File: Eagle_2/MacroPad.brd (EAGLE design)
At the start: 70.8 x 62.2 mm, 40 parts, among them SW00 SWITCH-SMD-EVQP-P2602W, SW01 KEYSWITCH-PLAIN-MX-1U, SW02 KEYSWITCH-PLAIN-MX-1U, SW03 KEYSWITCH-PLAIN-MX-1U, SW04 KEYSWITCH-PLAIN-MX-1U, SW05 KEYSWITCH-PLAIN-MX-1U, SW06 KEYSWITCH-PLAIN-MX-1U, SW07 KEYSWITCH-PLAIN-MX-1U, SW08 KEYSWITCH-PLAIN-MX-1U, SW09 KEYSWITCH-PLAIN-MX-1U, SW10 KEYSWITCH-PLAIN-MX-1U, SW11 KEYSWITCH-PLAIN-MX-1U, SW12 KEYSWITCH-PLAIN-MX-1U

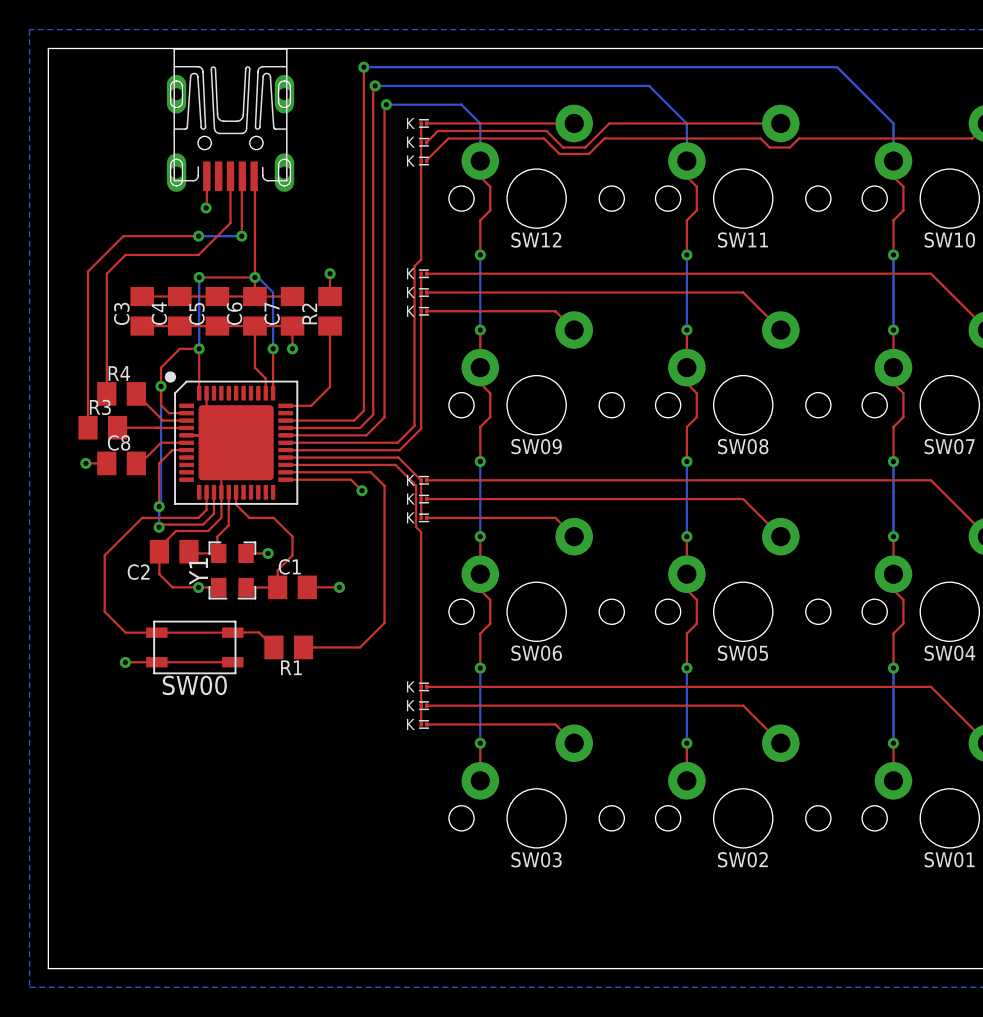
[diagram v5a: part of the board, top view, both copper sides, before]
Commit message: Components routed in compressed area
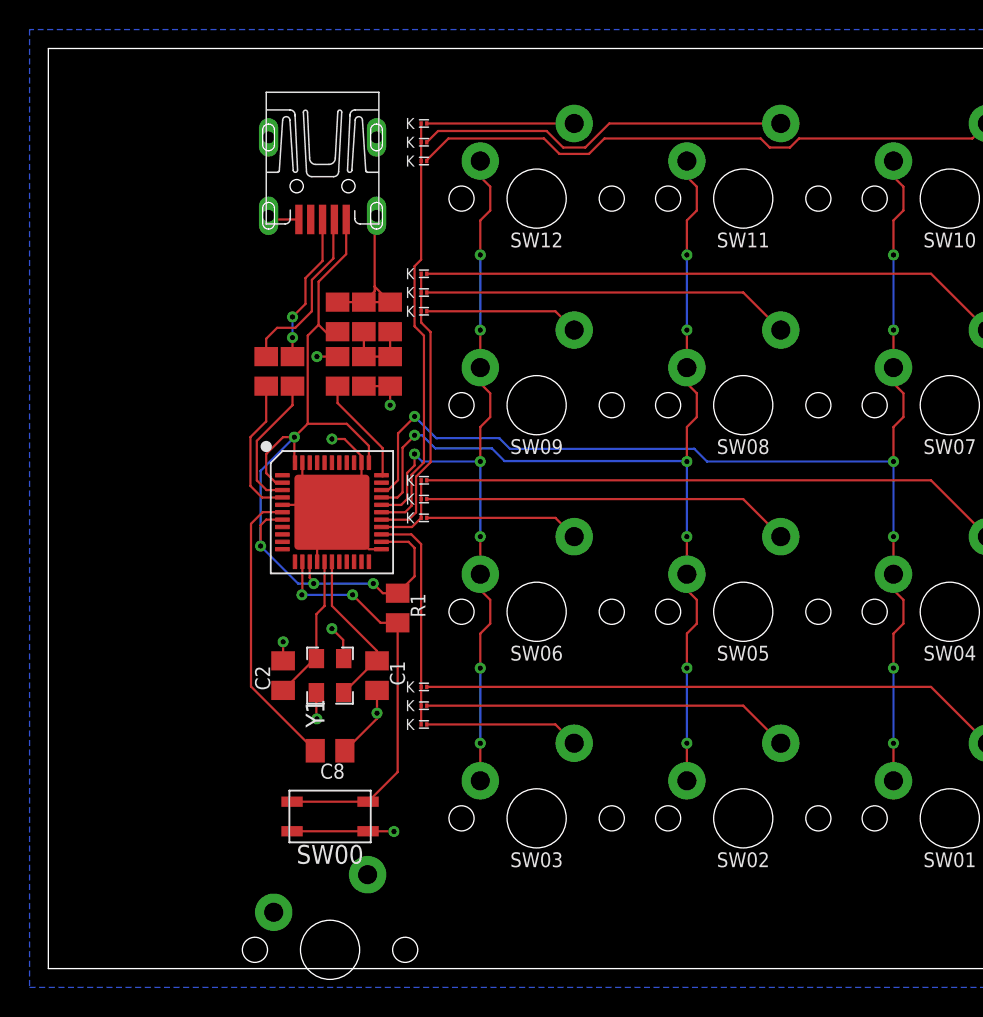
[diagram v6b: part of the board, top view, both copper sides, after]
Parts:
- added U$2: KEYSWITCH-PLAIN-MX-1U, Keyboard:MX-1U
- moved C8 24.0 mm to (19.1, 14.7), turned to 180 degrees
- moved C3 15.0 mm to (21.3, 44.1), turned to 270 degrees
- moved SW00 14.6 mm to (19.1, 10.3)
- moved C4 14.2 mm to (23.1, 44.1), turned to 270 degrees
- moved R3 11.7 mm to (14.7, 40.4), turned to 270 degrees
- moved R4 11.7 mm to (16.5, 40.4), turned to 270 degrees
- moved C2 11.2 mm to (15.9, 19.8), turned to 90 degrees
- moved Y1 9.71 mm to (19.1, 19.8)
- moved C6 8.41 mm to (21.3, 40.4)
- moved C1 8.26 mm to (22.2, 19.8), turned to 270 degrees
- moved C5 8.14 mm to (19.6, 44.1), turned to 270 degrees
- moved U$1 8.00 mm to (19.2, 30.9)
- moved R1 7.83 mm to (23.6, 24.4), turned to 270 degrees
- moved C7 7.75 mm to (23.1, 40.4)
- moved USB1 6.87 mm to (18.5, 59.3)
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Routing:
- net N$10: track 112.3 -> 83.5 mm
- net N$40: track 96.8 -> 68.5 mm
- net N$16: track 81.4 -> 53.4 mm
- net VCC: track 88.5 -> 65.5 mm, vias 7 -> 4
- net UCAP: track 3.98 -> 19.6 mm
- net N$7: track 26.0 -> 11.9 mm, vias 2 -> 0
- net N$5: track 21.1 -> 10.1 mm, vias 0 -> 2
- net N$14: track 25.7 -> 15.1 mm
- net N$26: track 12.3 -> 5.48 mm
- net N$6: track 4.14 -> 9.75 mm
- net N$8: track 5.07 -> 9.68 mm
- net UGND: track 64.0 -> 60.0 mm, vias 9 -> 8
- net N$1: track 6.55 -> 10.0 mm
- net N$3: track 25.6 -> 27.6 mm, vias 0 -> 2
- net N$38: track 29.8 -> 28.9 mm
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
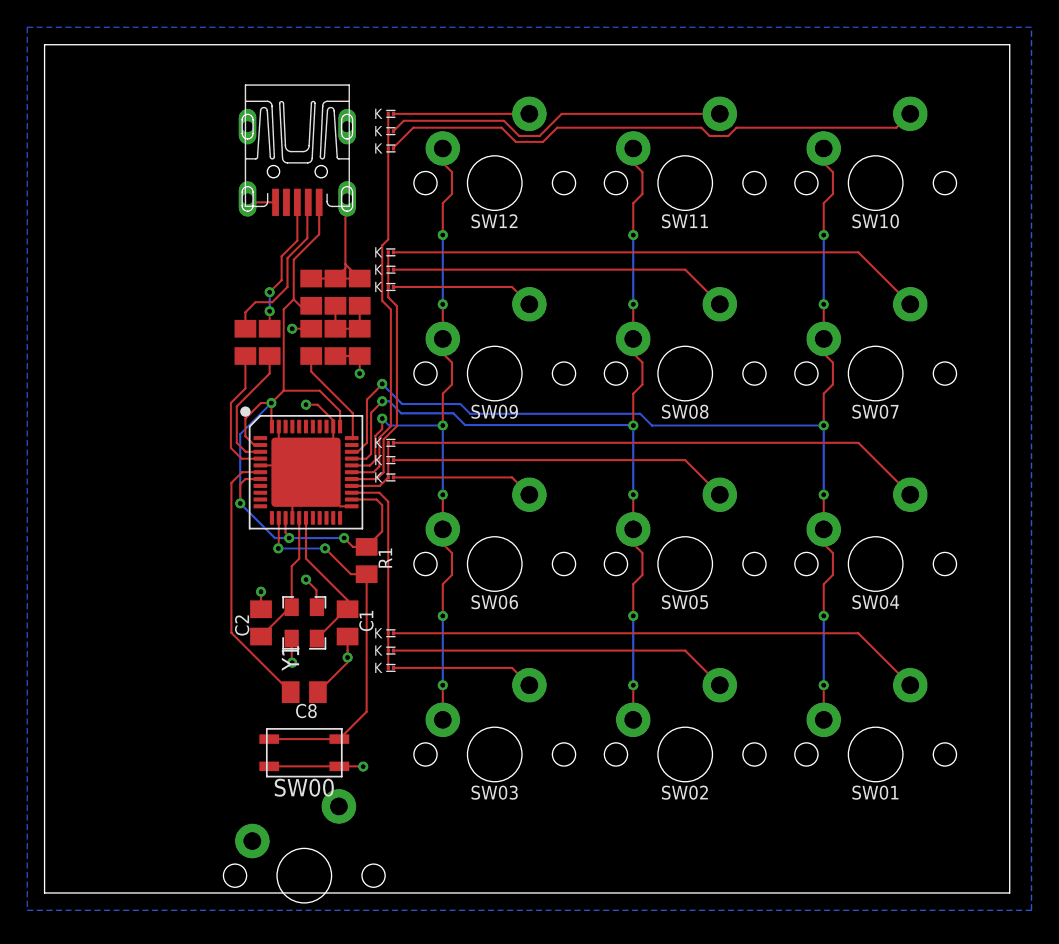
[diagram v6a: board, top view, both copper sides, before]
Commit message: Shrink board
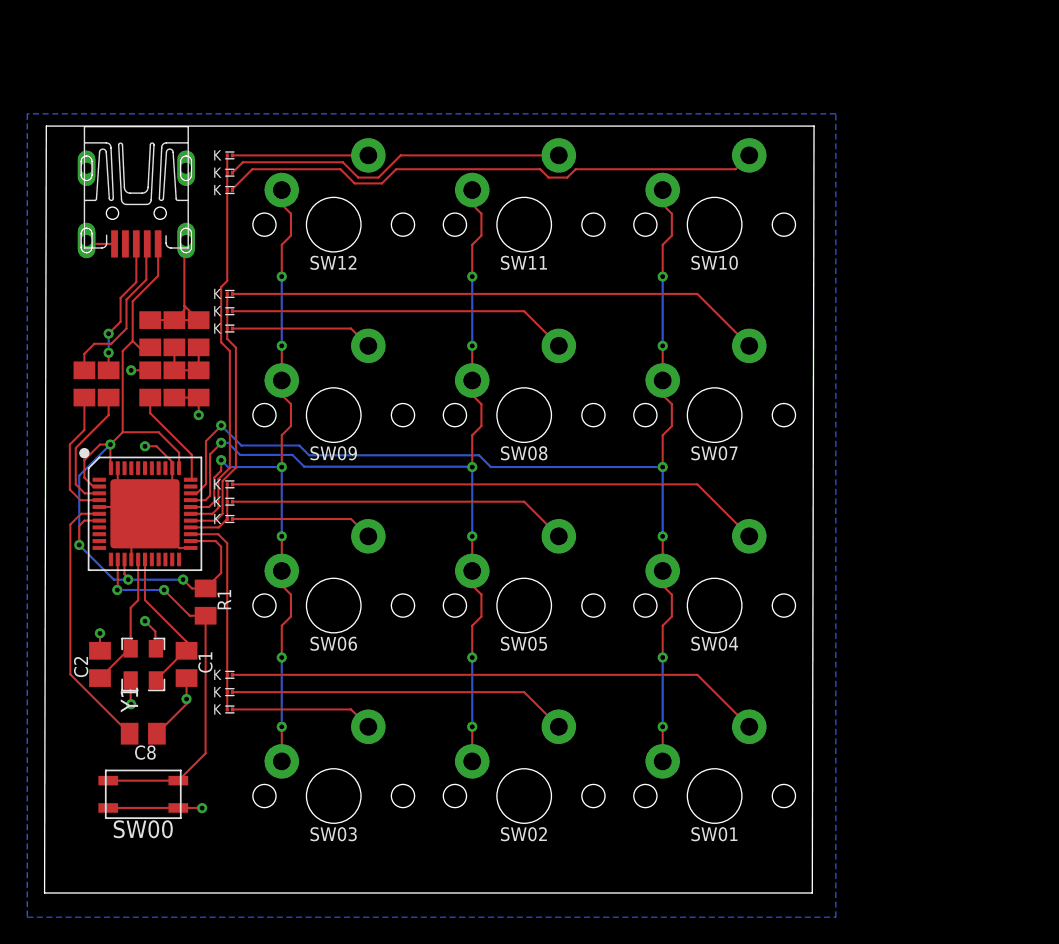
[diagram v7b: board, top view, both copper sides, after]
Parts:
- removed U$2: KEYSWITCH-PLAIN-MX-1U, Keyboard:MX-1U
- moved SW03 12.2 mm to (21.2, 7.11)
- moved SW09 12.2 mm to (21.2, 35.1)
- moved SW12 12.2 mm to (21.2, 49.0)
- moved C1 12.2 mm to (10.4, 16.8)
- moved R4 12.2 mm to (4.70, 37.3)
- moved SW06 12.2 mm to (21.2, 21.1)
- moved C2 12.2 mm to (4.06, 16.8)
- moved C4 12.2 mm to (11.3, 41.0)
- moved C5 12.2 mm to (7.75, 41.0)
- moved C7 12.2 mm to (11.3, 37.3)
- moved C8 12.2 mm to (7.24, 11.7)
- moved R1 12.2 mm to (11.8, 21.3)
- moved R2 12.2 mm to (7.75, 37.3)
- moved R3 12.2 mm to (2.92, 37.3)
- moved SW00 12.2 mm to (7.24, 7.24)
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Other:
- board size 70.8 x 62.2 mm -> 56.4 x 56.3 mm

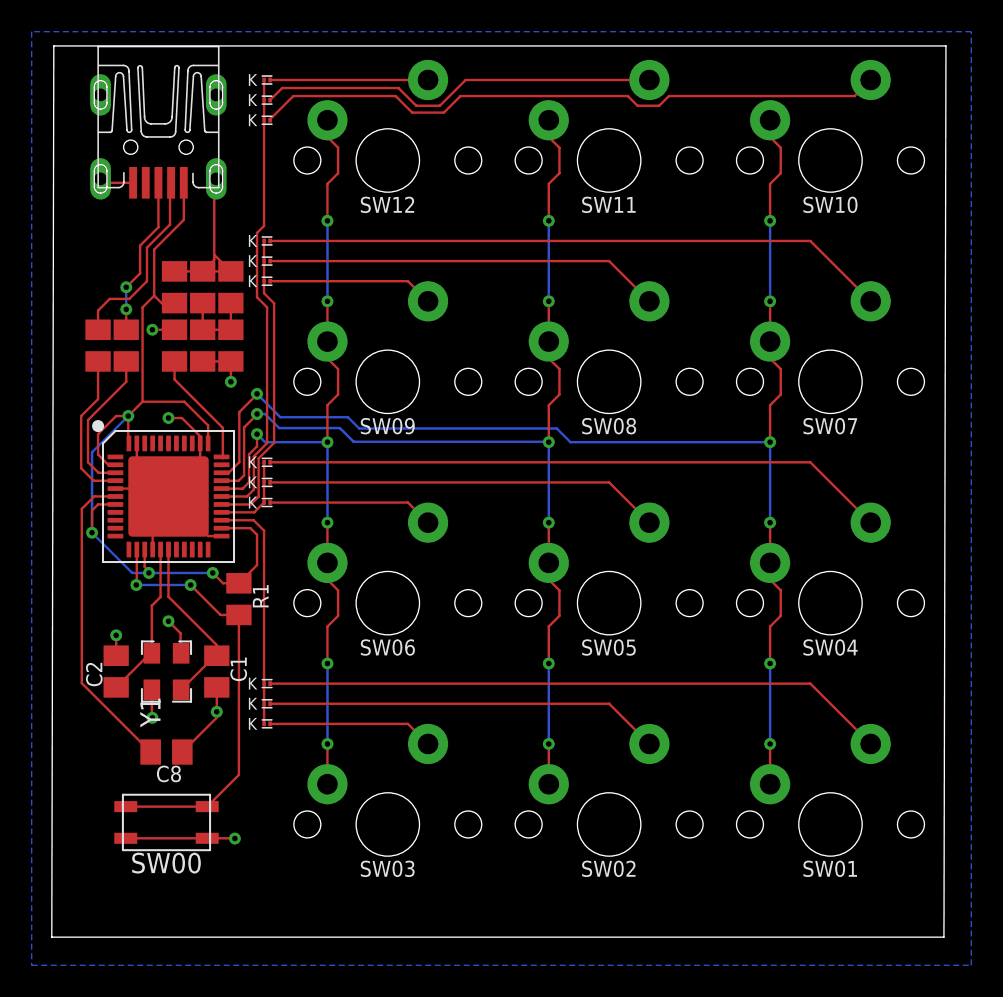
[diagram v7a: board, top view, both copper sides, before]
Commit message: Redone schematic with smaller capacitors, fixed decoupling capacitors, and adjusted trace sizes
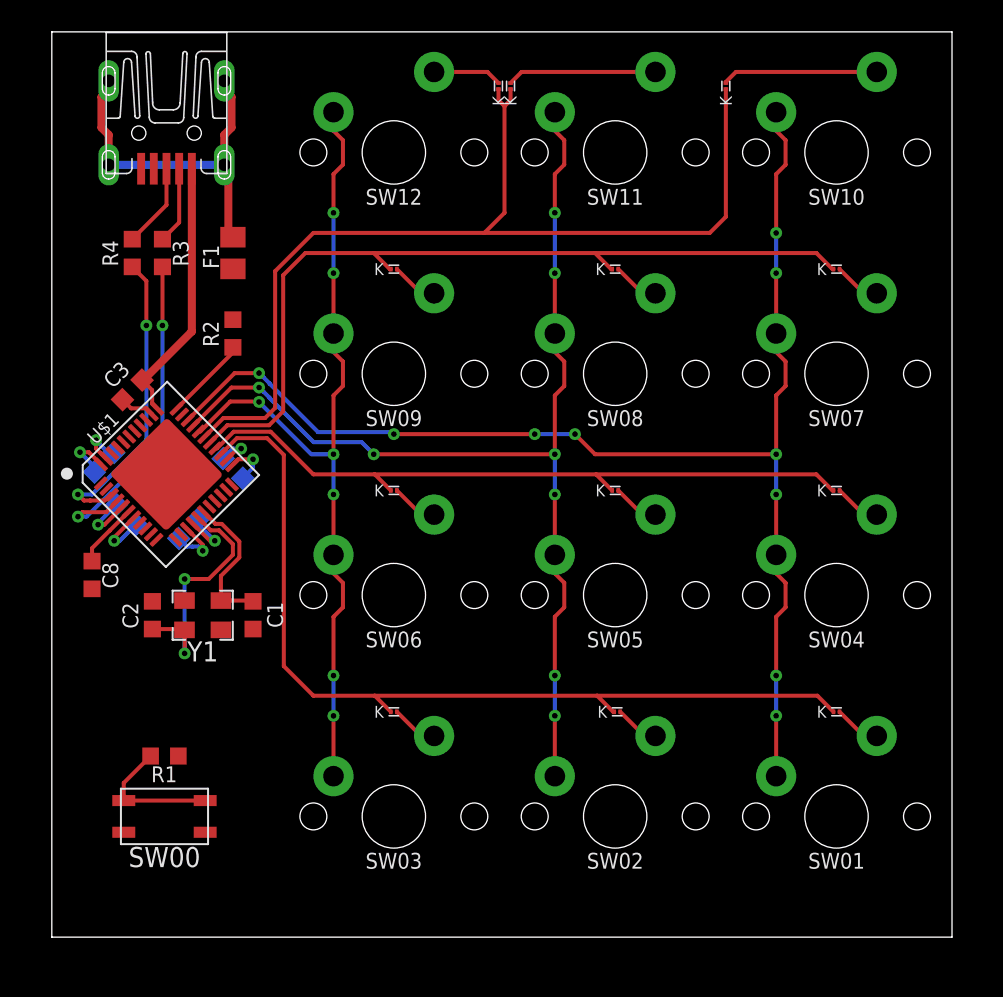
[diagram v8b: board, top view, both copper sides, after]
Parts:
- added F1: (no value), USB:F0805
- C1, C2, C3, C4, C5, C6, C7, C8: device Components:C0805 -> Components:C0603
- R1, R2, R3, R4: device Components:R0805 -> Components:R0603
- moved D1 36.0 mm to (49.5, 14.2)
- moved D4 36.0 mm to (49.5, 28.2)
- moved D7 36.0 mm to (49.5, 42.2)
- moved D10 29.0 mm to (42.5, 53.7), turned to 90 degrees
- moved D2 22.1 mm to (35.7, 14.2)
- moved D5 22.0 mm to (35.6, 28.2)
- moved D8 22.0 mm to (35.6, 42.2)
- moved C4 15.8 mm to (4.70, 26.7), flipped to the bottom, turned to 45 degrees
- moved D11 15.4 mm to (29.0, 53.7), turned to 90 degrees
- moved D12 14.6 mm to (28.2, 53.7), turned to 90 degrees
- moved C8 12.1 mm to (2.54, 22.9), turned to 270 degrees
- moved C5 11.9 mm to (3.30, 30.0), flipped to the bottom, turned to 135 degrees
- moved C6 11.6 mm to (8.64, 25.8), flipped to the bottom, turned to 135 degrees
- moved R1 11.0 mm to (7.11, 11.4), turned to 180 degrees
- moved D3 8.04 mm to (21.6, 14.2)
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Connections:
- new net GND: F1.1
- new net N$11: F1.2, USB1.SHIELD@1, USB1.SHIELD@2, USB1.SHIELD@3, USB1.SHIELD@4
- net N$1: now also C2.2; no longer C2.1
- net N$2: now also C1.2; no longer C1.1
- net N$4: now also R2.2; no longer R2.1
- net UCAP: now also C8.1; no longer C8.2
- net UGND: now also C1.1, C2.1, C3.2, C4.2, C5.2, C6.2, C7.2, C8.2, R2.1; no longer C1.2, C2.2, C3.1, C4.1, C5.1, C6.1, C7.1, C8.1, R2.2, USB1.SHIELD@1, USB1.SHIELD@2, USB1.SHIELD@3, USB1.SHIELD@4
- net VCC: now also C3.1, C4.1, C5.1, C6.1, C7.1; no longer C3.2, C4.2, C5.2, C6.2, C7.2
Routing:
- net UGND: track 60.0 -> 16.3 mm, vias 8 -> 4
- net N$14: track 15.1 -> 57.0 mm
- net N$26: track 5.48 -> 43.9 mm
- net N$18: track 39.5 -> 2.98 mm
- net N$9: track 39.5 -> 2.98 mm
- net N$27: track 39.5 -> 2.98 mm
- net VCC: track 65.5 -> 30.7 mm
- net N$38: track 28.9 -> 62.8 mm
- net N$32: track 19.4 -> 52.8 mm
- net N$36: track 40.4 -> 9.84 mm
- net N$11: track 0.00 -> 23.4 mm
- net N$12: track 25.0 -> 2.85 mm
- net N$21: track 25.0 -> 2.98 mm
- net N$30: track 25.0 -> 2.98 mm
- net N$3: track 27.6 -> 8.76 mm, vias 2 -> 0
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- removed copper zone on layer 16, net UGND
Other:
- board size 56.4 x 56.3 mm -> 56.8 x 57.1 mm
